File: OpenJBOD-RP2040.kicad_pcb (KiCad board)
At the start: 4 copper layers, 72.6 x 170 mm, 119 parts, among them J1 ATX-24, J2 Bus_PCI_Express_x1, J3 Conn_02x02_Counter_Clockwise, J6 HR911105A, J8 USB_B_Micro, J9 TEMP1, Q1 MMBT3904, Q2 MMBT3904, SW1 SW_Push, SW2 SW_Push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

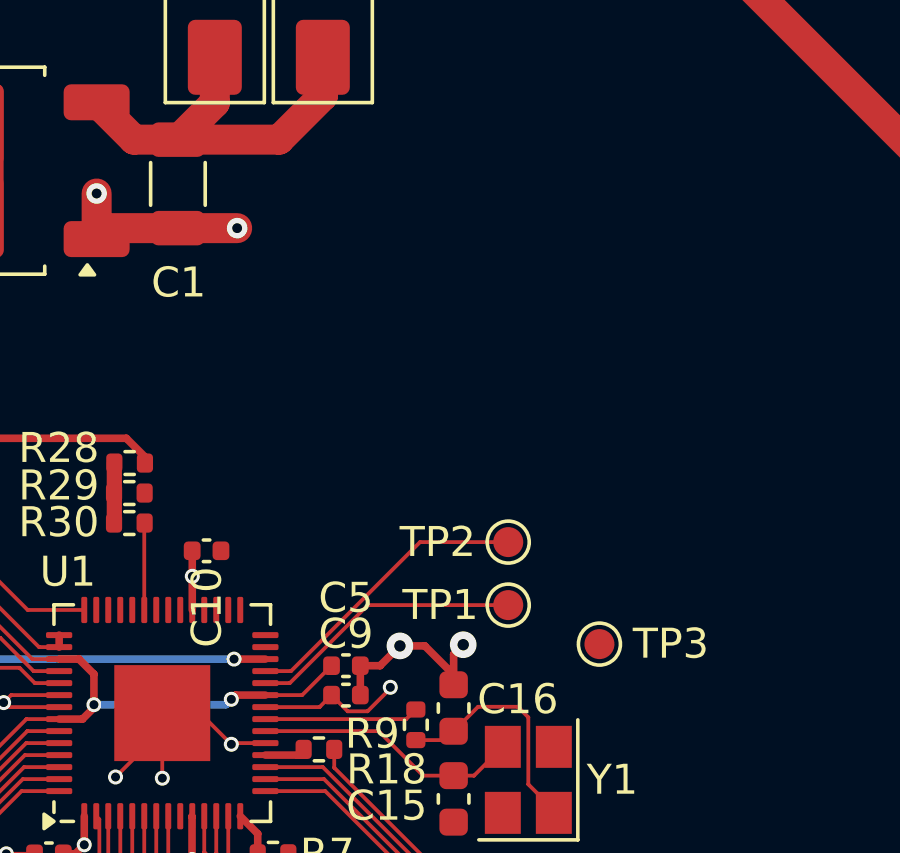
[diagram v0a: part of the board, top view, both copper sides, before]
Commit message: added uart header
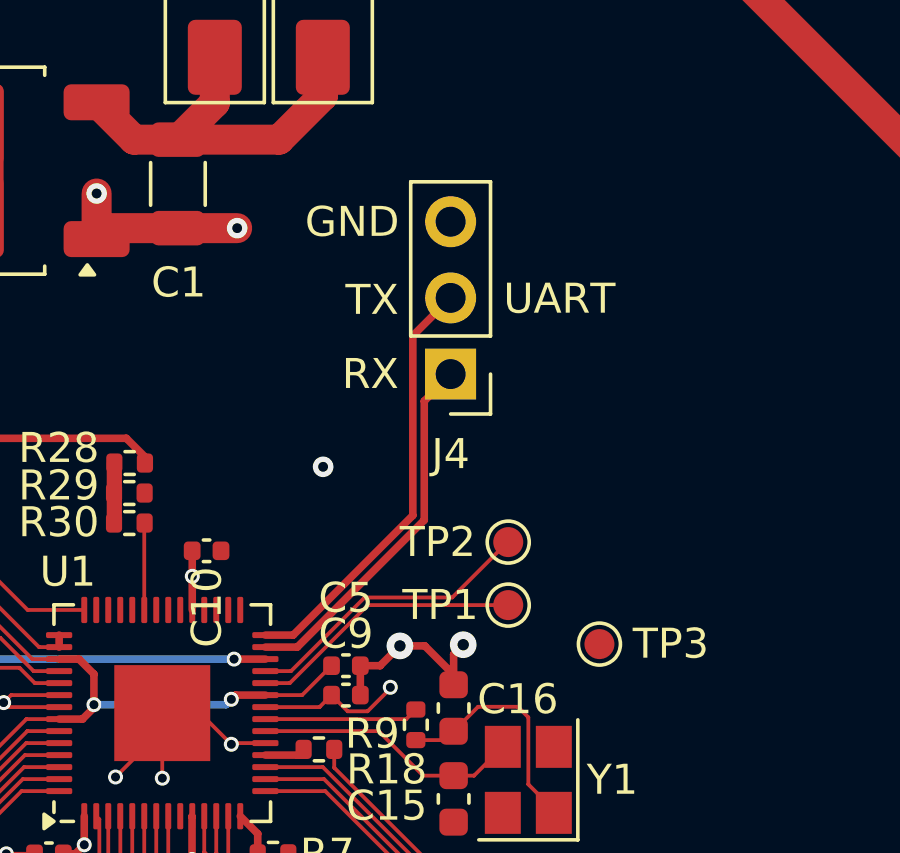
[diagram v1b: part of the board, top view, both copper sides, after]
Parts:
- added J4: UART, Connector_PinHeader_2.54mm:PinHeader_1x03_P2.54mm_Vertical, F.Cu at (128.5, 107.8)
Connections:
- U1 pad 27: unconnected-(U1-GPIO16-Pad27) -> /UART_TX
- U1 pad 28: unconnected-(U1-GPIO17-Pad28) -> /UART_RX
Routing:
- net /UART_RX: track 0.00 -> 14.3 mm
- net /UART_TX: track 0.00 -> 12.3 mm
- net GND: vias 52 -> 53
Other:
- board text added: "RX"
- board text added: "TX"
- board text added: "UART"

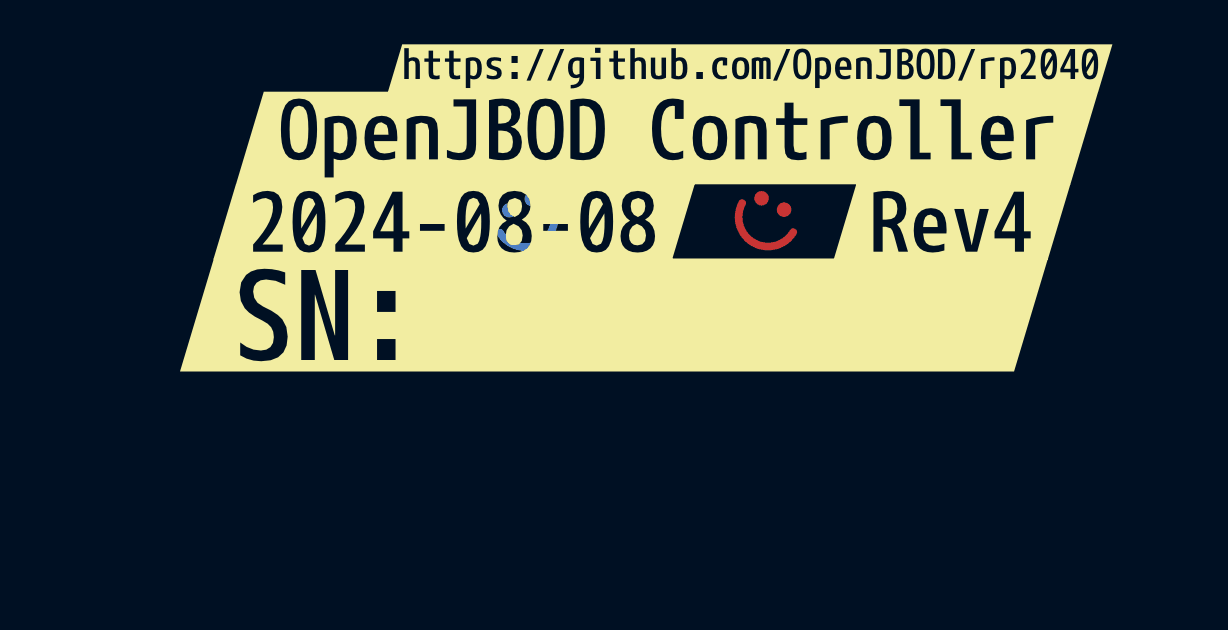
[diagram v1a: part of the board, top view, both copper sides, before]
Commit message: remove serial number graphic in favor of digital sn
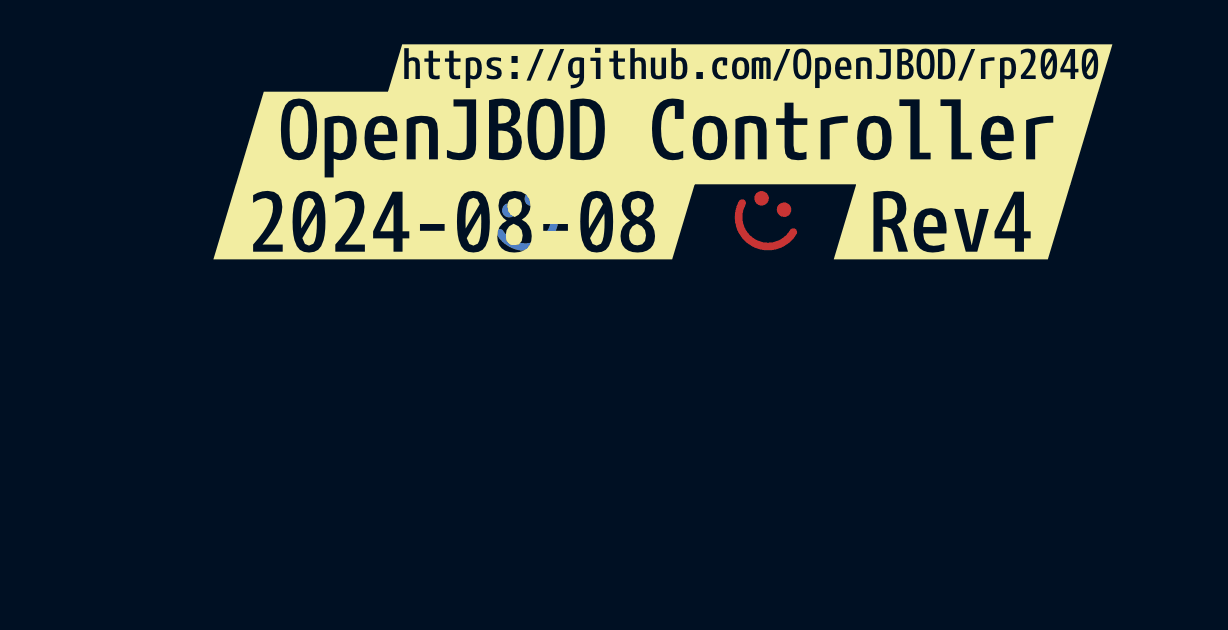
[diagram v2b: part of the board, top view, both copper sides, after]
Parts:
- removed kibuzzard-66B485B8 (x2): G***, kibuzzard-66B485B8
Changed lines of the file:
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@@
 		)
 	)
-	(footprint "kibuzzard-66B485B8"
-		(layer "F.Cu")
-		(at 114.229762 177.57)
-		(descr "Generated with KiBuzzard")
-		(tags "kb_params=eyJBbGlnbm1lbnRDaG9pY2UiOiAiQ2VudGVyIiwgIkNhcExlZnRDaG9pY2UiOiAiLyIsICJDYXBSaWdodENob2ljZSI6ICIvIiwgIkZvbnRDb21ib0JveCI6ICJtcGx1cy0xbW4tbWVkaXVtIiwgIkhlaWdodEN0cmwiOiAzLjAsICJMYXllckNvbWJvQm94IjogIkYuU2lsa1MiLCAiTGluZVNwYWNpbmdDdHJsIjogMS41LCAiTXVsdGlMaW5lVGV4dCI6ICJTTjoiLCAiUGFkZGluZ0JvdHRvbUN0cmwiOiAxLjAsICJQYWRkaW5nTGVmdEN0cmwiOiAyLjUsICJQYWRkaW5nUmlnaHRDdHJsIjogNjAuMiwgIlBhZGRpbmdUb3BDdHJsIjogMS4wLCAiV2lkdGhDdHJsIjogMC4wLCAiYWR2YW5jZWRDaGVja2JveCI6IGZhbHNlLCAiaW5saW5lRm9ybWF0VGV4dGJveCI6IGZhbHNlLCAibGluZW92ZXJTdHlsZUNob2ljZSI6ICJTcXVhcmUiLCAibGluZW92ZXJUaGlja25lc3NDdHJsIjogMX0=")
-		(property "Reference" "kibuzzard-66B485B8"
-			(at 0 -4.931562 0)
-			(layer "F.SilkS")
-			(hide yes)
-			(effects
-				(font
-					(size 0.001 0.001)
-				)
-			)
-		)
-		(property "Value" "G***"
-			(at 0 4.931562 0)
-			(layer "F.SilkS")
-			(hide yes)
-			(effects
-				(font
-					(size 0.001 0.001)
-				)
-			)
-		)
-		(property "Footprint" "kibuzzard-66B485B8"
-			(at 0 0 0)
-			(unlocked yes)
-			(layer "F.Fab")
-			(hide yes)
-			(effects
-				(font
-					(size 1.27 1.27)
-				)
-			)
-		)
-		(property "Datasheet" ""
-			(at 0 0 0)
-			(unlocked yes)
-			(layer "F.Fab")
-			(hide yes)
-			(effects
-				(font
-					(size 1.27 1.27)
-				)
-			)
-		)
-		(property "Description" ""
-			(at 0 0 0)
-			(unlocked yes)
-			(layer "F.Fab")
-			(hide yes)
-			(effects
-				(font
-					(size 1.27 1.27)
-				)
-			)
-		)
-		(attr board_only exclude_from_pos_files exclude_from_bom)
-		(fp_poly
-			(pts
-				(xy -12.479452 -1.883562) (xy -13.335616 -1.883562) (xy -14.465753 1.883562) (xy -13.335616 1.883562)
-				(xy -12.479452 1.883562) (xy -11.760274 1.883562) (xy -11.760274 1.541096) (xy -12.015068 1.519178)
-				(xy -12.247945 1.453425) (xy -12.458904 1.343836) (xy -12.458904 0.916438) (xy -12.242009 1.06484)
-				(xy -12.013242 1.153881) (xy -11.772603 1.183562) (xy -11.589726 1.155308) (xy -11.452055 1.070548)
-				(xy -11.365753 0.931336) (xy -11.336986 0.739726) (xy -11.359075 0.556849) (xy -11.425342 0.410959)
-				(xy -11.542979 0.290753) (xy -11.719178 0.184932) (xy -11.971005 0.053425) (xy -12.16758 -0.083562)
-				(xy -12.308904 -0.226027) (xy -12.436815 -0.468493) (xy -12.479452 -0.760274) (xy -12.425514 -1.089041)
-				(xy -12.263699 -1.335616) (xy -12.099543 -1.449772) (xy -11.894749 -1.518265) (xy -11.649315 -1.541096)
-				(xy -11.410046 -1.527397) (xy -11.179909 -1.486301) (xy -10.958904 -1.417808) (xy -10.958904 -1.006849)
-				(xy -11.27637 -1.139384) (xy -11.59589 -1.183562) (xy -11.775685 -1.156849) (xy -11.912329 -1.076712)
-				(xy -11.99863 -0.949315) (xy -12.027397 -0.780822) (xy -11.990868 -0.572146) (xy -11.881279 -0.406393)
-				(xy -11.69863 -0.283562) (xy -11.418721 -0.142466) (xy -11.203653 0.00137) (xy -11.053425 0.147945)
-				(xy -10.92089 0.401712) (xy -10.876712 0.719178) (xy -10.912055 1.015068) (xy -11.018082 1.245205)
-				(xy -11.194795 1.409589) (xy -11.442192 1.508219) (xy -11.760274 1.541096) (xy -11.760274 1.883562)
-				(xy -10.424658 1.883562) (xy -10.424658 1.5) (xy -10.424658 -1.5) (xy -9.947945 -1.5) (xy -9.306849 0.678082)
-				(xy -9.294521 0.678082) (xy -9.294521 -1.5) (xy -8.863014 -1.5) (xy -8.863014 1.5) (xy -9.323288 1.5)
-				(xy -9.964384 -0.678082) (xy -9.972603 -0.678082) (xy -9.972603 1.5) (xy -10.424658 1.5) (xy -10.424658 1.883562)
-				(xy -7.89726 1.883562) (xy -7.89726 -0.10274) (xy -7.89726 -0.80137) (xy -7.280822 -0.80137) (xy -7.280822 -0.10274)
-				(xy -7.89726 -0.10274) (xy -7.89726 1.883562) (xy -7.89726 1.5) (xy -7.89726 0.80137) (xy -7.280822 0.80137)
-				(xy -7.280822 1.5) (xy -7.89726 1.5) (xy -7.89726 1.883562) (xy -7.280822 1.883562) (xy 13.335616 1.883562)
-				(xy 14.465753 -1.883562) (xy 13.335616 -1.883562) (xy -7.280822 -1.883562) (xy -12.479452 -1.883562)
-			)
-			(stroke
-				(width 0)
-				(type solid)
-			)
-			(fill solid)
-			(layer "F.SilkS")
-		)
-	)
 	(footprint "Capacitor_SMD:C_0402_1005Metric"
 		(layer "F.Cu")
@@
 		)
 		(fp_text user "${REFERENCE}"
-			(at 0 2.54 270)
+			(at 0 2.54 -90)
 			(layer "F.Fab")
 			(effects
@@
 		)
 	)
-	(footprint "kibuzzard-66B485B8"
-		(layer "B.Cu")
-		(at 116.408826 177.59 180)
-		(descr "Generated with KiBuzzard")
-		(tags "kb_params=eyJBbGlnbm1lbnRDaG9pY2UiOiAiQ2VudGVyIiwgIkNhcExlZnRDaG9pY2UiOiAiLyIsICJDYXBSaWdodENob2ljZSI6ICIvIiwgIkZvbnRDb21ib0JveCI6ICJtcGx1cy0xbW4tbWVkaXVtIiwgIkhlaWdodEN0cmwiOiAzLjAsICJMYXllckNvbWJvQm94IjogIkYuU2lsa1MiLCAiTGluZVNwYWNpbmdDdHJsIjogMS41LCAiTXVsdGlMaW5lVGV4dCI6ICJTTjoiLCAiUGFkZGluZ0JvdHRvbUN0cmwiOiAxLjAsICJQYWRkaW5nTGVmdEN0cmwiOiAyLjUsICJQYWRkaW5nUmlnaHRDdHJsIjogNjAuMiwgIlBhZGRpbmdUb3BDdHJsIjogMS4wLCAiV2lkdGhDdHJsIjogMC4wLCAiYWR2YW5jZWRDaGVja2JveCI6IGZhbHNlLCAiaW5saW5lRm9ybWF0VGV4dGJveCI6IGZhbHNlLCAibGluZW92ZXJTdHlsZUNob2ljZSI6ICJTcXVhcmUiLCAibGluZW92ZXJUaGlja25lc3NDdHJsIjogMX0=")
-		(property "Reference" "kibuzzard-66B485B8"
-			(at 0 4.931562 180)
-			(layer "B.SilkS")
-			(hide yes)
-			(effects
-				(font
-					(size 0.001 0.001)
-				)
-				(justify mirror)
-			)
-		)
-		(property "Value" "G***"
-			(at 0 -4.931562 180)
-			(layer "B.SilkS")
-			(hide yes)
-			(effects
-				(font
-					(size 0.001 0.001)
-				)
-				(justify mirror)
-			)
-		)
-		(property "Footprint" "kibuzzard-66B485B8"
-			(at 0 0 0)
-			(unlocked yes)
-			(layer "B.Fab")
-			(hide yes)
-			(effects
-				(font
-					(size 1.27 1.27)
-				)
-				(justify mirror)
-			)
-		)
-		(property "Datasheet" ""
-			(at 0 0 0)
-			(unlocked yes)
-			(layer "B.Fab")
-			(hide yes)
-			(effects
-				(font
-					(size 1.27 1.27)
-				)
-				(justify mirror)
-			)
-		)
-		(property "Description" ""
-			(at 0 0 0)
-			(unlocked yes)
-			(layer "B.Fab")
-			(hide yes)
-			(effects
-				(font
-					(size 1.27 1.27)
-				)
-				(justify mirror)
-			)
-		)
-		(attr board_only exclude_from_pos_files exclude_from_bom)
-		(fp_poly
-			(pts
-				(xy -12.479452 1.883562) (xy -13.335616 1.883562) (xy -14.465753 -1.883562) (xy -13.335616 -1.883562)
-				(xy -12.479452 -1.883562) (xy -11.760274 -1.883562) (xy -11.760274 -1.541096) (xy -12.015068 -1.519178)
-				(xy -12.247945 -1.453425) (xy -12.458904 -1.343836) (xy -12.458904 -0.916438) (xy -12.242009 -1.06484)
-				(xy -12.013242 -1.153881) (xy -11.772603 -1.183562) (xy -11.589726 -1.155308) (xy -11.452055 -1.070548)
-				(xy -11.365753 -0.931336) (xy -11.336986 -0.739726) (xy -11.359075 -0.556849) (xy -11.425342 -0.410959)
-				(xy -11.542979 -0.290753) (xy -11.719178 -0.184932) (xy -11.971005 -0.053425) (xy -12.16758 0.083562)
-				(xy -12.308904 0.226027) (xy -12.436815 0.468493) (xy -12.479452 0.760274) (xy -12.425514 1.089041)
-				(xy -12.263699 1.335616) (xy -12.099543 1.449772) (xy -11.894749 1.518265) (xy -11.649315 1.541096)
-				(xy -11.410046 1.527397) (xy -11.179909 1.486301) (xy -10.958904 1.417808) (xy -10.958904 1.006849)
-				(xy -11.27637 1.139384) (xy -11.59589 1.183562) (xy -11.775685 1.156849) (xy -11.912329 1.076712)
-				(xy -11.99863 0.949315) (xy -12.027397 0.780822) (xy -11.990868 0.572146) (xy -11.881279 0.406393)
-				(xy -11.69863 0.283562) (xy -11.418721 0.142466) (xy -11.203653 -0.00137) (xy -11.053425 -0.147945)
-				(xy -10.92089 -0.401712) (xy -10.876712 -0.719178) (xy -10.912055 -1.015068) (xy -11.018082 -1.245205)
-				(xy -11.194795 -1.409589) (xy -11.442192 -1.508219) (xy -11.760274 -1.541096) (xy -11.760274 -1.883562)
-				(xy -10.424658 -1.883562) (xy -10.424658 -1.5) (xy -10.424658 1.5) (xy -9.947945 1.5) (xy -9.306849 -0.678082)
-				(xy -9.294521 -0.678082) (xy -9.294521 1.5) (xy -8.863014 1.5) (xy -8.863014 -1.5) (xy -9.323288 -1.5)
-				(xy -9.964384 0.678082) (xy -9.972603 0.678082) (xy -9.972603 -1.5) (xy -10.424658 -1.5) (xy -10.424658 -1.883562)
-				(xy -7.89726 -1.883562) (xy -7.89726 0.10274) (xy -7.89726 0.80137) (xy -7.280822 0.80137) (xy -7.280822 0.10274)
-				(xy -7.89726 0.10274) (xy -7.89726 -1.883562) (xy -7.89726 -1.5) (xy -7.89726 -0.80137) (xy -7.280822 -0.80137)
-				(xy -7.280822 -1.5) (xy -7.89726 -1.5) (xy -7.89726 -1.883562) (xy -7.280822 -1.883562) (xy 13.335616 -1.883562)
-				(xy 14.465753 1.883562) (xy 13.335616 1.883562) (xy -7.280822 1.883562) (xy -12.479452 1.883562)
-			)
-			(stroke
-				(width 0)
-				(type solid)
-			)
-			(fill solid)
-			(layer "B.SilkS")
-		)
-	)
 	(footprint "Symbol:OSHW-Logo2_14.6x12mm_Copper"
 		(layer "B.Cu")
@@
 	)
 	(gr_text "JLCJLCJLCJLC"
-		(at 129.938588 180.99 0)
+		(at 129.83 177.08 0)
 		(layer "B.SilkS")
 		(effects

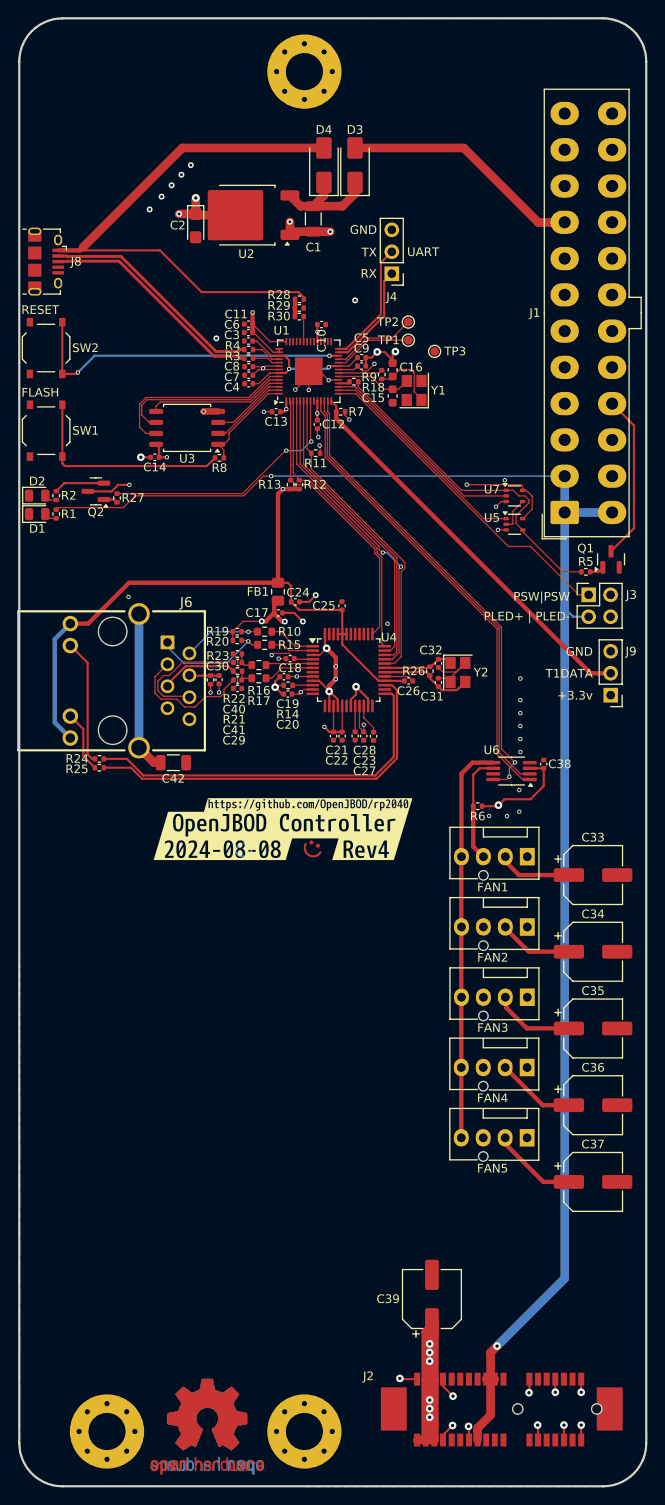
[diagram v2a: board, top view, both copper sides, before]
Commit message: Rev4
Bunch of small changes, namely:
Add onboard DS18B20 probe for more accurate temp readings without external hardware.
Rename T1DATA to T2DATA to still allow external probes.
Add USB power sensing circuit.
Add SR latch for PS_ON# handling
Add J4 UART header.
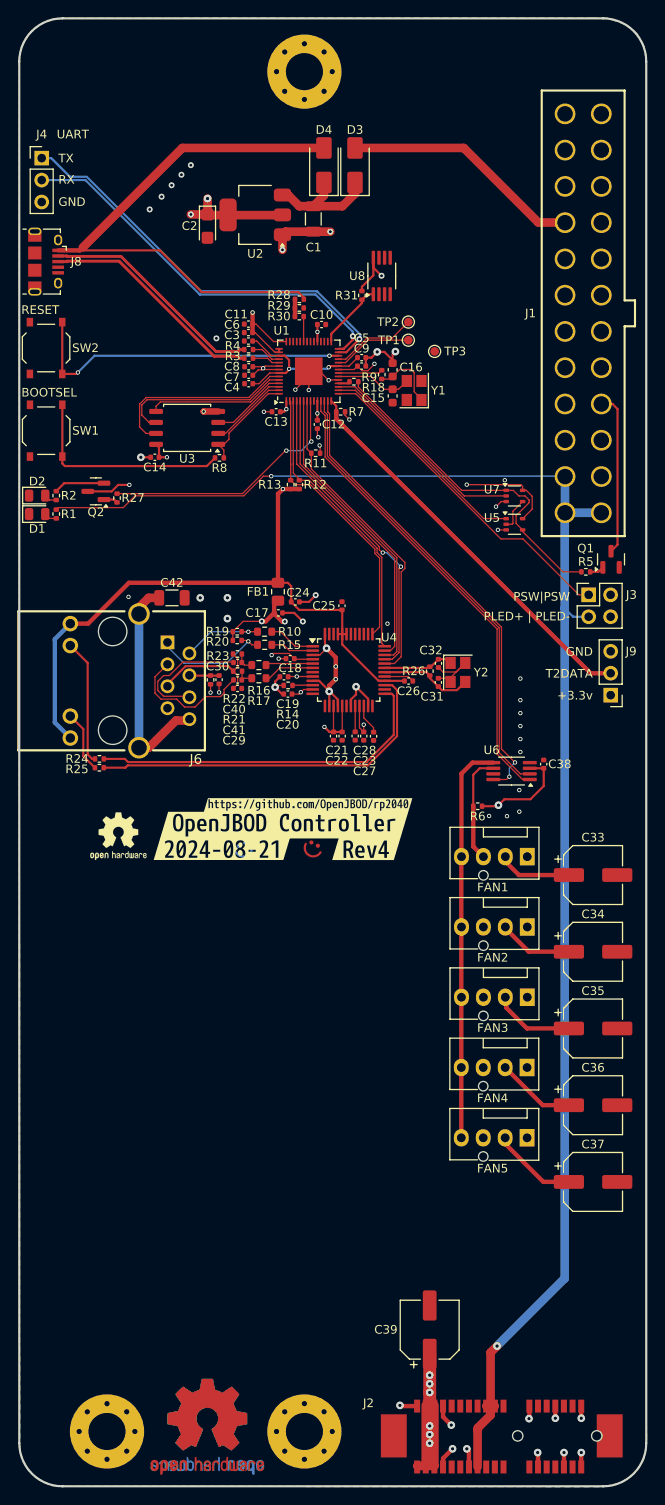
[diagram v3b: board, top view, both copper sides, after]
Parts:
- removed kibuzzard-66B48408 (x2): G***, kibuzzard-66B48408
- added R31: 4.7k, Resistor_SMD:R_0402_1005Metric, F.Cu at (125.0, 110.3)
- added REF**: OSHW-Logo2_7.3x6mm_SilkScreen, Symbol:OSHW-Logo2_7.3x6mm_SilkScreen, F.Cu at (96.8, 172.9)
- added REF**: OSHW-Logo2_7.3x6mm_SilkScreen, Symbol:OSHW-Logo2_7.3x6mm_SilkScreen, B.Cu at (96.8, 172.9)
- added U8: DS18B20U, Package_SO:MSOP-8_3x3mm_P0.65mm, F.Cu at (127.3, 108.1)
- added kibuzzard-66C5D9FB: G***, kibuzzard-66C5D9FB, F.Cu at (108.8, 174.4)
- added kibuzzard-66C5DA48: G***, kibuzzard-66C5DA48, B.Cu at (121.9, 174.5)
- D3, D4: value SS34 -> SS14
- J1: footprint Connector_Molex:Molex_Mini-Fit_Jr_5566-24A_2x12_P4.20mm_Vertical -> OpenJBOD_Library:CONN-TH_M4202V-2X12P
- U2: value UZ1085L-33 -> AMS1117-3.3; footprint Package_TO_SOT_SMD:TO-252-2 -> Package_TO_SOT_SMD:SOT-223-3_TabPin2
- moved J4 42.7 mm to (87.9, 94.4), turned to 0 degrees
- moved J1 23.2 mm to (150.6, 112.4)
- moved C42 19.1 mm to (103.0, 145.3)
- moved C39 3.56 mm to (132.8, 230.1)
- moved J2 3.12 mm to (126.7, 234.4)
- moved C2 1.37 mm to (107.1, 102.3)
- moved U2 1.03 mm to (112.7, 101.0)
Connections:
- J6 pad 8: GND -> Earth
- J9 pad 2: /T1_DATA -> /T2_DATA
- R7 pad 1: /T1_DATA -> /T2_DATA
- U1 pad 14: /T1_DATA -> /T2_DATA
- U1 pad 29: unconnected-(U1-GPIO18-Pad29) -> /T1_DATA
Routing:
- net /T2_DATA: track 0.00 -> 46.3 mm
- net /T1_DATA: track 46.3 -> 7.90 mm
- net /UART_TX: track 12.3 -> 49.0 mm, vias 0 -> 1
- net /UART_RX: track 14.3 -> 46.3 mm, vias 0 -> 1
- net /+3.3vSB: track 208.8 -> 223.5 mm, vias 15 -> 16
- net GND: track 86.8 -> 100.8 mm, vias 53 -> 55
- net Earth: track 18.7 -> 26.3 mm
- net /+12v: track 73.6 -> 70.6 mm
- net /W5500/LINKn: track 43.5 -> 40.7 mm
- net /W5500/ACTn: track 45.1 -> 42.5 mm
- net /+3.3v: track 186.0 -> 187.9 mm
- net /+5vSB: track 13.2 -> 14.1 mm
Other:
- board text added: "BOOTSEL"
- board text added: "Rev4 production sponsored by:"
- board text added: "Riff.CC"
- board text added: "T2DATA"
- board text removed: "FLASH"
- board text removed: "T1DATA"
